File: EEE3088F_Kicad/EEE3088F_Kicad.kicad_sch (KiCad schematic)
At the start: 4 parts, among them IC1 AS5600-ASOT, U5 DRV5032FCDBZR, U6 MCP9700T-E/TT

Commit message: I have made my changes
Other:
- added sheet MicrocontrollerInterface (MicrocontrollerInterface.kicad_sch)
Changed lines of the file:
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@@
     (pin "3")
     (instances
-      (project "Sensor Modules"
+      (project "EEE3088F_Kicad"
         (path "/6f03c876-746d-4bbb-b455-2f8bb16ffc56"
           (reference "U5") (unit 1)
@@
     (pin "1")
     (instances
-      (project "Sensor Modules"
+      (project "EEE3088F_Kicad"
         (path "/6f03c876-746d-4bbb-b455-2f8bb16ffc56"
           (reference "#PWR04") (unit 1)
@@
     (pin "3")
     (instances
-      (project "Sensor Modules"
+      (project "EEE3088F_Kicad"
         (path "/6f03c876-746d-4bbb-b455-2f8bb16ffc56"
           (reference "U6") (unit 1)
@@
     (pin "8")
     (instances
-      (project "Sensor Modules"
+      (project "EEE3088F_Kicad"
         (path "/6f03c876-746d-4bbb-b455-2f8bb16ffc56"
           (reference "IC1") (unit 1)
@@
     (pin "1")
     (instances
-      (project "Sensor Modules"
+      (project "EEE3088F_Kicad"
         (path "/6f03c876-746d-4bbb-b455-2f8bb16ffc56"
           (reference "#PWR06") (unit 1)
@@
     (pin "1")
     (instances
-      (project "Sensor Modules"
+      (project "EEE3088F_Kicad"
         (path "/6f03c876-746d-4bbb-b455-2f8bb16ffc56"
           (reference "#PWR01") (unit 1)
@@
     (pin "1")
     (instances
-      (project "Sensor Modules"
+      (project "EEE3088F_Kicad"
         (path "/6f03c876-746d-4bbb-b455-2f8bb16ffc56"
           (reference "#PWR02") (unit 1)
@@
     (pin "2")
     (instances
-      (project "Sensor Modules"
+      (project "EEE3088F_Kicad"
         (path "/6f03c876-746d-4bbb-b455-2f8bb16ffc56"
           (reference "C1") (unit 1)
@@
     (pin "1")
     (instances
-      (project "Sensor Modules"
+      (project "EEE3088F_Kicad"
         (path "/6f03c876-746d-4bbb-b455-2f8bb16ffc56"
           (reference "#PWR05") (unit 1)
@@
     (pin "1")
     (instances
-      (project "Sensor Modules"
+      (project "EEE3088F_Kicad"
         (path "/6f03c876-746d-4bbb-b455-2f8bb16ffc56"
           (reference "#PWR03") (unit 1)
         )
+      )
+    )
+  )
+  (sheet (at 46.99 48.26) (size 74.93 39.37) (fields_autoplaced)
+    (stroke (width 0.1524) (type solid))
+    (fill (color 0 0 0 0.0000))
+    (property "Sheetname" "MicrocontrollerInterface" (at 46.99 47.5484 0)
+      (effects (font (size 1.27 1.27)) (justify left bottom))
+    )
+    (property "Sheetfile" "MicrocontrollerInterface.kicad_sch" (at 46.99 88.2146 0)
+      (effects (font (size 1.27 1.27)) (justify left top))
+    )
+    (instances
+      (project "EEE3088F_Kicad"
+        (path "/6f03c876-746d-4bbb-b455-2f8bb16ffc56" (page "3"))
       )
     )
@@
     )
     (instances
-      (project "Sensor Modules"
+      (project "EEE3088F_Kicad"
         (path "/6f03c876-746d-4bbb-b455-2f8bb16ffc56" (page "2"))
       )

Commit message: I have made changes for power
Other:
- added sheet Power (Power.kicad_sch)
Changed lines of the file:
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@@
+    )
+  )
+  (sheet (at 43.18 113.03) (size 77.47 44.45) (fields_autoplaced)
+    (stroke (width 0.1524) (type solid))
+    (fill (color 0 0 0 0.0000))
+    (property "Sheetname" "Power" (at 43.18 112.3184 0)
+      (effects (font (size 1.27 1.27)) (justify left bottom))
+    )
+    (property "Sheetfile" "Power.kicad_sch" (at 43.18 158.0646 0)
+      (effects (font (size 1.27 1.27)) (justify left top))
+    )
+    (instances
+      (project "EEE3088F_Kicad"
+        (path "/6f03c876-746d-4bbb-b455-2f8bb16ffc56" (page "4"))
+      )
     )
   )

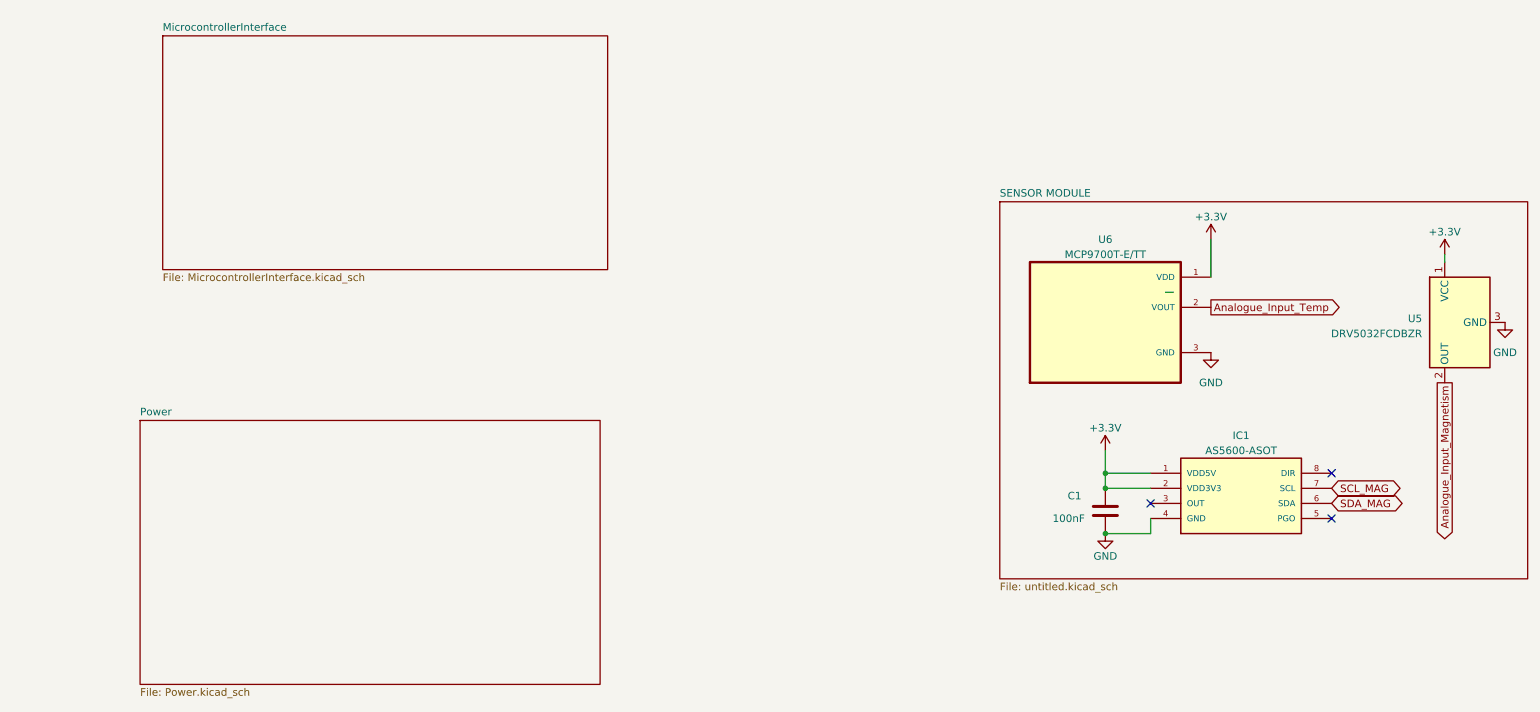
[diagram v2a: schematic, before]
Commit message: Wuzzup Team!!! I have modified my sensor module part and added it to the schematic.
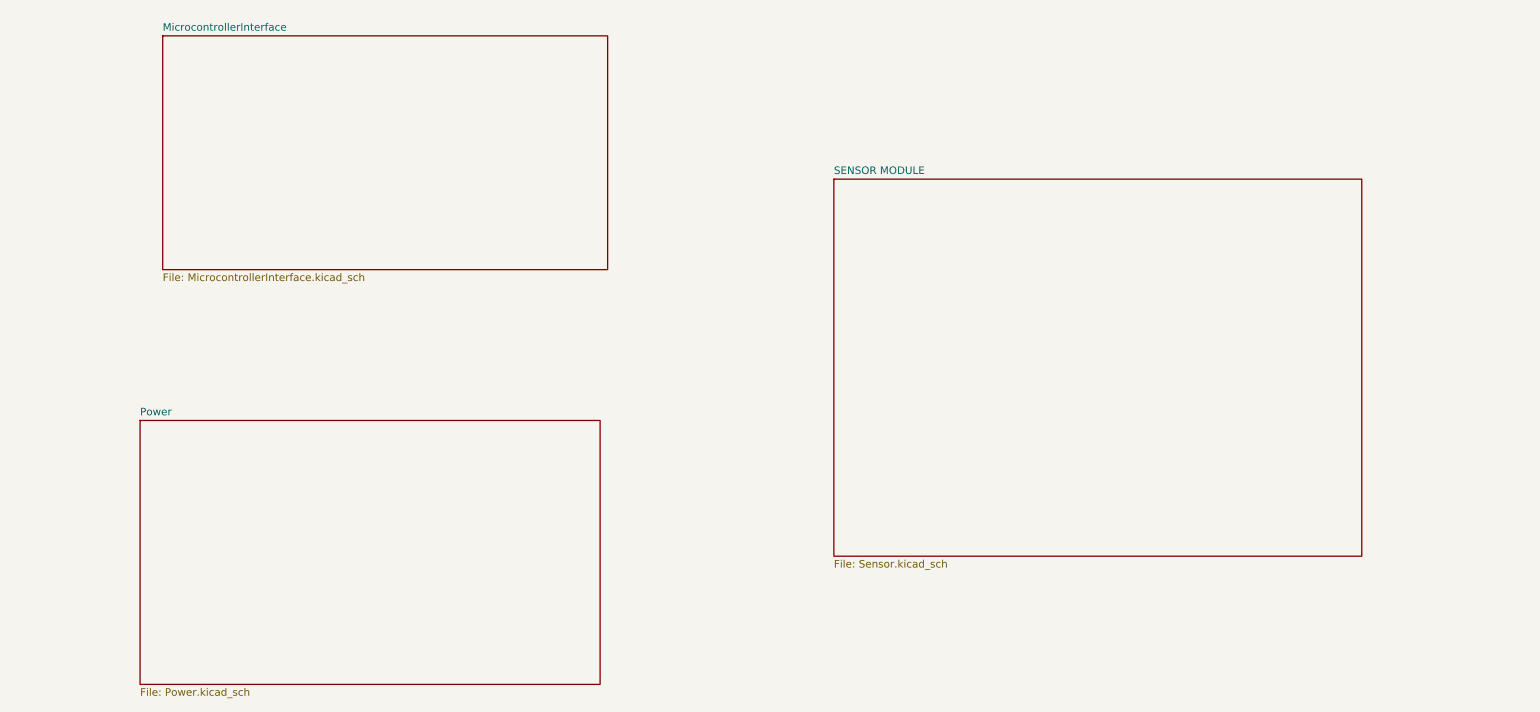
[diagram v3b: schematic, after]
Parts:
- removed C1: 100nF, symbol Device:C
- removed IC1: AS5600-ASOT, SOIC127P600X175-8N, symbol AS5600-ASOT:AS5600-ASOT
- removed U5: DRV5032FCDBZR, DRV5032FCDBZR:SOT95P237X112-3N, symbol Sensor_Magnetic:DRV5033FAxDBZ
- removed U6: MCP9700T-E/TT, MCP9700T-ETT:SOT95P237X112-3N, symbol MCP9700T-E_TT:MCP9700T-E/TT
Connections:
- no-connect marks 3 -> 0
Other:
- sheet SENSOR MODULE: file untitled.kicad_sch -> Sensor.kicad_sch

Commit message: added the external connections between subsystems
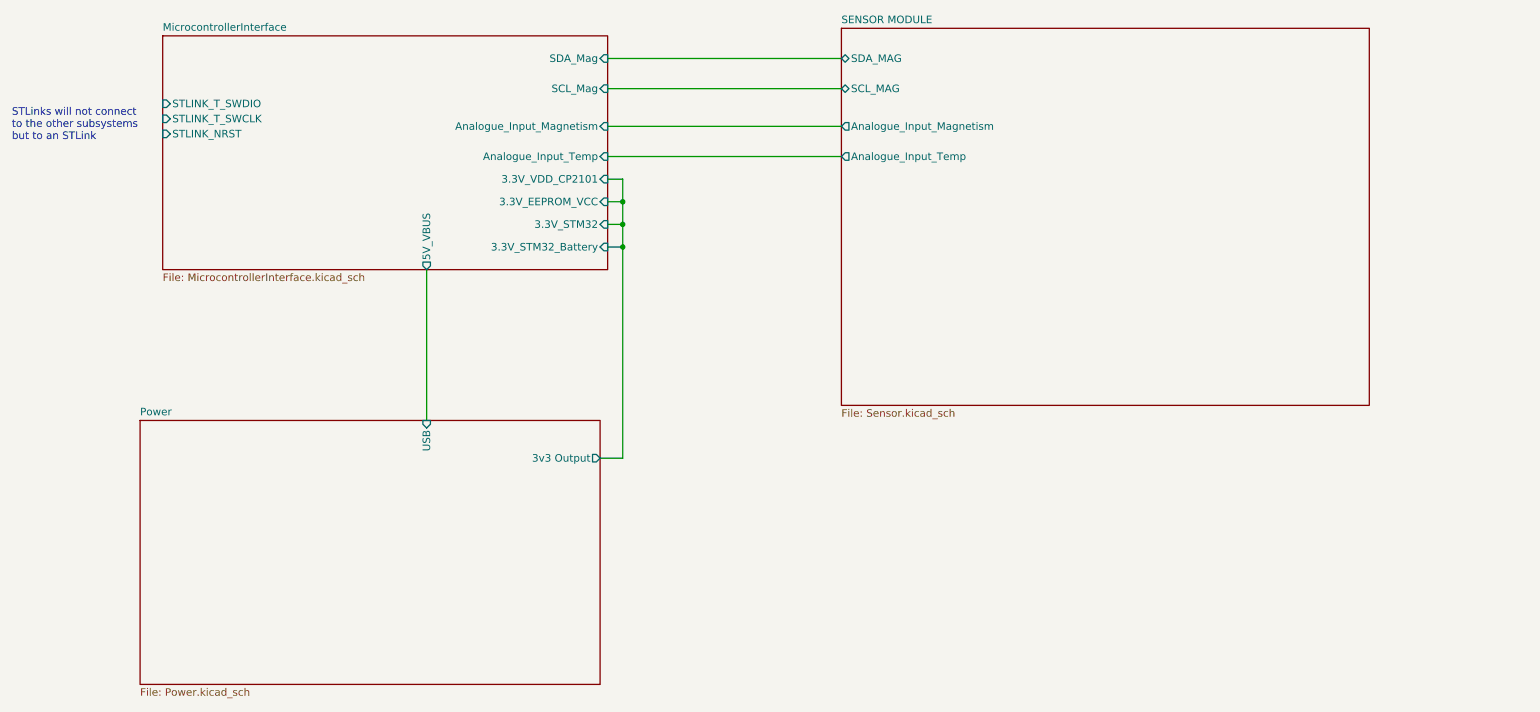
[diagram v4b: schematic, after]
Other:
- sheet MicrocontrollerInterface ports: added 3.3V_EEPROM_VCC, 3.3V_STM32, 3.3V_STM32_Battery, 3.3V_VDD_CP2101, 5V_VBUS, Analogue_Input_Magnetism, Analogue_Input_Temp, SCL_Mag, SDA_Mag, STLINK_NRST, STLINK_T_SWCLK, STLINK_T_SWDIO; removed none
- sheet Power ports: added 3v3 Output, USB; removed none
- sheet SENSOR MODULE ports: added Analogue_Input_Magnetism, Analogue_Input_Temp, SCL_MAG, SDA_MAG; removed none
- note added: "STLinks will not connect to the other subsystems but to an STLink"
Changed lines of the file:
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@@
 (kicad_sch (version 20230121) (generator eeschema)
   (paper "A4")
+  (junction (at 124.46 76.2) (diameter 0) (color 0 0 0 0)
+  )
+  (junction (at 124.46 80.01) (diameter 0) (color 0 0 0 0)
+  )
+  (junction (at 124.46 83.82) (diameter 0) (color 0 0 0 0)
+  )
+  (wire (pts (xy 124.46 80.01) (xy 124.46 83.82))
+    (stroke (width 0) (type default))
+  )
+  (wire (pts (xy 121.92 83.82) (xy 124.46 83.82))
+    (stroke (width 0) (type default))
+  )
+  (wire (pts (xy 121.92 72.39) (xy 124.46 72.39))
+    (stroke (width 0) (type default))
+  )
+  (wire (pts (xy 121.92 80.01) (xy 124.46 80.01))
+    (stroke (width 0) (type default))
+  )
+  (wire (pts (xy 121.92 52.07) (xy 161.29 52.07))
+    (stroke (width 0) (type default))
+  )
+  (wire (pts (xy 124.46 119.38) (xy 124.46 83.82))
+    (stroke (width 0) (type default))
+  )
+  (wire (pts (xy 124.46 76.2) (xy 124.46 80.01))
+    (stroke (width 0) (type default))
+  )
+  (wire (pts (xy 120.65 119.38) (xy 124.46 119.38))
+    (stroke (width 0) (type default))
+  )
+  (wire (pts (xy 121.92 76.2) (xy 124.46 76.2))
+    (stroke (width 0) (type default))
+  )
+  (wire (pts (xy 91.44 87.63) (xy 91.44 113.03))
+    (stroke (width 0) (type default))
+  )
+  (wire (pts (xy 121.92 68.58) (xy 161.29 68.58))
+    (stroke (width 0) (type default))
+  )
+  (wire (pts (xy 124.46 72.39) (xy 124.46 76.2))
+    (stroke (width 0) (type default))
+  )
+  (wire (pts (xy 121.92 57.15) (xy 161.29 57.15))
+    (stroke (width 0) (type default))
+  )
+  (wire (pts (xy 121.92 63.5) (xy 161.29 63.5))
+    (stroke (width 0) (type default))
+  )
+  (text "STLinks will not connect \nto the other subsystems\nbut to an STLink"
+    (at 21.59 66.04 0)
+    (effects (font (size 1.27 1.27)) (justify left bottom))
+  )
   (sheet (at 43.18 113.03) (size 77.47 44.45) (fields_autoplaced)
     (stroke (width 0.1524) (type solid))
@@
     (property "Sheetfile" "Power.kicad_sch" (at 43.18 158.0646 0)
       (effects (font (size 1.27 1.27)) (justify left top))
+    )
+    (pin "3v3 Output" output (at 120.65 119.38 0)
+      (effects (font (size 1.27 1.27)) (justify right))
+    )
+    (pin "USB" input (at 91.44 113.03 90)
+      (effects (font (size 1.27 1.27)) (justify right))
     )
     (instances
@@
       (effects (font (size 1.27 1.27)) (justify left top))
     )
+    (pin "3.3V_EEPROM_VCC" input (at 121.92 76.2 0)
+      (effects (font (size 1.27 1.27)) (justify right))
+    )
+    (pin "5V_VBUS" output (at 91.44 87.63 270)
+      (effects (font (size 1.27 1.27)) (justify left))
+    )
+    (pin "3.3V_STM32" input (at 121.92 80.01 0)
+      (effects (font (size 1.27 1.27)) (justify right))
+    )
+    (pin "3.3V_STM32_Battery" input (at 121.92 83.82 0)
+      (effects (font (size 1.27 1.27)) (justify right))
+    )
+    (pin "STLINK_NRST" input (at 46.99 64.77 180)
+      (effects (font (size 1.27 1.27)) (justify left))
+    )
+    (pin "STLINK_T_SWCLK" input (at 46.99 62.23 180)
+      (effects (font (size 1.27 1.27)) (justify left))
+    )
+    (pin "Analogue_Input_Magnetism" input (at 121.92 63.5 0)
+      (effects (font (size 1.27 1.27)) (justify right))
+    )
+    (pin "STLINK_T_SWDIO" input (at 46.99 59.69 180)
+      (effects (font (size 1.27 1.27)) (justify left))
+    )
+    (pin "Analogue_Input_Temp" input (at 121.92 68.58 0)
+      (effects (font (size 1.27 1.27)) (justify right))
+    )
+    (pin "SDA_Mag" input (at 121.92 52.07 0)
+      (effects (font (size 1.27 1.27)) (justify right))
+    )
+    (pin "SCL_Mag" input (at 121.92 57.15 0)
+      (effects (font (size 1.27 1.27)) (justify right))
+    )
+    (pin "3.3V_VDD_CP2101" input (at 121.92 72.39 0)
+      (effects (font (size 1.27 1.27)) (justify right))
+    )
     (instances
       (project "EEE3088F_Kicad"
@@
     )
   )
-  (sheet (at 160.02 72.39) (size 88.9 63.5) (fields_autoplaced)
+  (sheet (at 161.29 46.99) (size 88.9 63.5) (fields_autoplaced)
     (stroke (width 0.1524) (type solid))
     (fill (color 0 0 0 0.0000))
-    (property "Sheetname" "SENSOR MODULE" (at 160.02 71.6784 0)
+    (property "Sheetname" "SENSOR MODULE" (at 161.29 46.2784 0)
       (effects (font (size 1.27 1.27)) (justify left bottom))
     )
-    (property "Sheetfile" "Sensor.kicad_sch" (at 160.02 136.4746 0)
+    (property "Sheetfile" "Sensor.kicad_sch" (at 161.29 111.0746 0)
       (effects (font (size 1.27 1.27)) (justify left top))
     )
+    (pin "SDA_MAG" bidirectional (at 161.29 52.07 180)
+      (effects (font (size 1.27 1.27)) (justify left))
+    )
+    (pin "SCL_MAG" bidirectional (at 161.29 57.15 180)
+      (effects (font (size 1.27 1.27)) (justify left))
+    )
+    (pin "Analogue_Input_Magnetism" output (at 161.29 63.5 180)
+      (effects (font (size 1.27 1.27)) (justify left))
+    )
+    (pin "Analogue_Input_Temp" output (at 161.29 68.58 180)
+      (effects (font (size 1.27 1.27)) (justify left))
+    )
     (instances
